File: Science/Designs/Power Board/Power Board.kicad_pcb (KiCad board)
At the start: 2 copper layers, 102.7 x 89.4 mm, 31 parts, among them P1 PWR_IN, P2 MOTOR_PWR_OUT, P3 MAIN_PWR_OUT, P4 I2C, P5 MOTOR_SW, P6 REG_12V, P7 REG_5V, U1 INA219, U2 INA219, U3 INA219

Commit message: squeezed
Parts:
- moved P7 1.78 mm to (165.4, 134.8)
- moved P3 1.78 mm to (165.4, 75.9)
- moved P6 1.78 mm to (165.4, 103.1)
- moved REF** 1.27 mm to (96.8, 106.7)
- moved REF** 1.27 mm to (96.8, 53.8)
- moved P1 0.92 mm to (108.5, 74.0)
- moved REF** 0.76 mm to (161.0, 53.1)
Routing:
- net +12V: track 80.2 -> 84.9 mm
- net +5V: track 62.8 -> 66.4 mm
- net /24V_IN: track 18.7 -> 15.6 mm
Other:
- board size 102.7 x 89.4 mm -> 99.4 x 89.4 mm

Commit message: Final changes
(I didn't save apparently)
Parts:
- moved G*** 6.59 mm to (157.2, 69.1)
- moved G*** 1.70 mm to (123.2, 73.2)
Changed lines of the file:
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@@
   )
   (module ScienceFootprints:Husky-0.50in (layer F.Cu)
-    (at 122.428 71.628)
+    (at 123.19 73.152)
     (fp_text reference G*** (at 0 0) (layer F.SilkS) hide
       (effects (font (thickness 0.3)))
@@
   )
   (module ScienceFootprints:Scarlet-0.25in (layer F.Cu)
-    (at 163.068 72.136)
+    (at 157.226 69.088)
     (fp_text reference G*** (at 0 0) (layer F.SilkS) hide
       (effects (font (thickness 0.3)))
@@
   (gr_line (start 191.008 133.096) (end 191.008 54.356) (layer Edge.Cuts) (width 0.15))
   (gr_line (start 96.266 138.176) (end 185.928 138.176) (layer Edge.Cuts) (width 0.15))
-  (gr_text I2C (at 152.654 61.976) (layer F.SilkS)
-    (effects (font (size 1.5 1.5) (thickness 0.3)))
-  )
-  (gr_text "Power Input" (at 98.044 66.04 90) (layer F.SilkS)
-    (effects (font (size 1.5 1.5) (thickness 0.3)))
-  )
-  (gr_text GND (at 111.76 75.184 180) (layer F.SilkS)
-    (effects (font (size 1.5 1.5) (thickness 0.3)))
-  )
-  (gr_text +24V (at 103.632 75.184 180) (layer F.SilkS)
-    (effects (font (size 1.5 1.5) (thickness 0.3)))
-  )
-  (gr_text "Science Power Distribution Board\nHusky Robotics 2018\nJaden B/Cai B" (at 147.32 71.628) (layer F.SilkS)
+  (gr_text I2C (at 157.734 59.182 90) (layer F.SilkS)
+    (effects (font (size 1.5 1.5) (thickness 0.3)))
+  )
+  (gr_text "Power Input" (at 98.806 66.04 90) (layer F.SilkS)
+    (effects (font (size 1.5 1.5) (thickness 0.3)))
+  )
+  (gr_text GND (at 112.776 75.184 180) (layer F.SilkS)
+    (effects (font (size 1.5 1.5) (thickness 0.3)))
+  )
+  (gr_text +24V (at 104.902 75.184 180) (layer F.SilkS)
+    (effects (font (size 1.5 1.5) (thickness 0.3)))
+  )
+  (gr_text "Science Power Distribution Board\nHusky Robotics 2018\nJaden B/Cai B" (at 140.716 68.072) (layer F.SilkS)
     (effects (font (size 1.5 1.5) (thickness 0.3)))
   )
@@
     (effects (font (size 1.5 1.5) (thickness 0.3)))
   )
-  (gr_text GND (at 164.592 122.936 90) (layer F.SilkS)
-    (effects (font (size 1.5 1.5) (thickness 0.3)))
-  )
-  (gr_text +5V (at 164.592 115.316 90) (layer F.SilkS)
-    (effects (font (size 1.5 1.5) (thickness 0.3)))
-  )
-  (gr_text +24V (at 164.592 99.568 90) (layer F.SilkS)
-    (effects (font (size 1.5 1.5) (thickness 0.3)))
-  )
-  (gr_text GND (at 164.592 91.44 90) (layer F.SilkS)
+  (gr_text GND (at 164.338 122.936 90) (layer F.SilkS)
+    (effects (font (size 1.5 1.5) (thickness 0.3)))
+  )
+  (gr_text +5V (at 164.338 115.316 90) (layer F.SilkS)
+    (effects (font (size 1.5 1.5) (thickness 0.3)))
+  )
+  (gr_text +24V (at 164.338 99.568 90) (layer F.SilkS)
+    (effects (font (size 1.5 1.5) (thickness 0.3)))
+  )
+  (gr_text GND (at 164.338 91.44 90) (layer F.SilkS)
     (effects (font (size 1.5 1.5) (thickness 0.3)))
   )
@@
     (effects (font (size 1.5 1.5) (thickness 0.3)))
   )
-  (gr_text GND (at 164.592 64.008 90) (layer F.SilkS)
-    (effects (font (size 1.5 1.5) (thickness 0.3)))
-  )
+  (gr_text GND (at 164.338 64.008 90) (layer F.SilkS)
+    (effects (font (size 1.5 1.5) (thickness 0.3)))
+  )

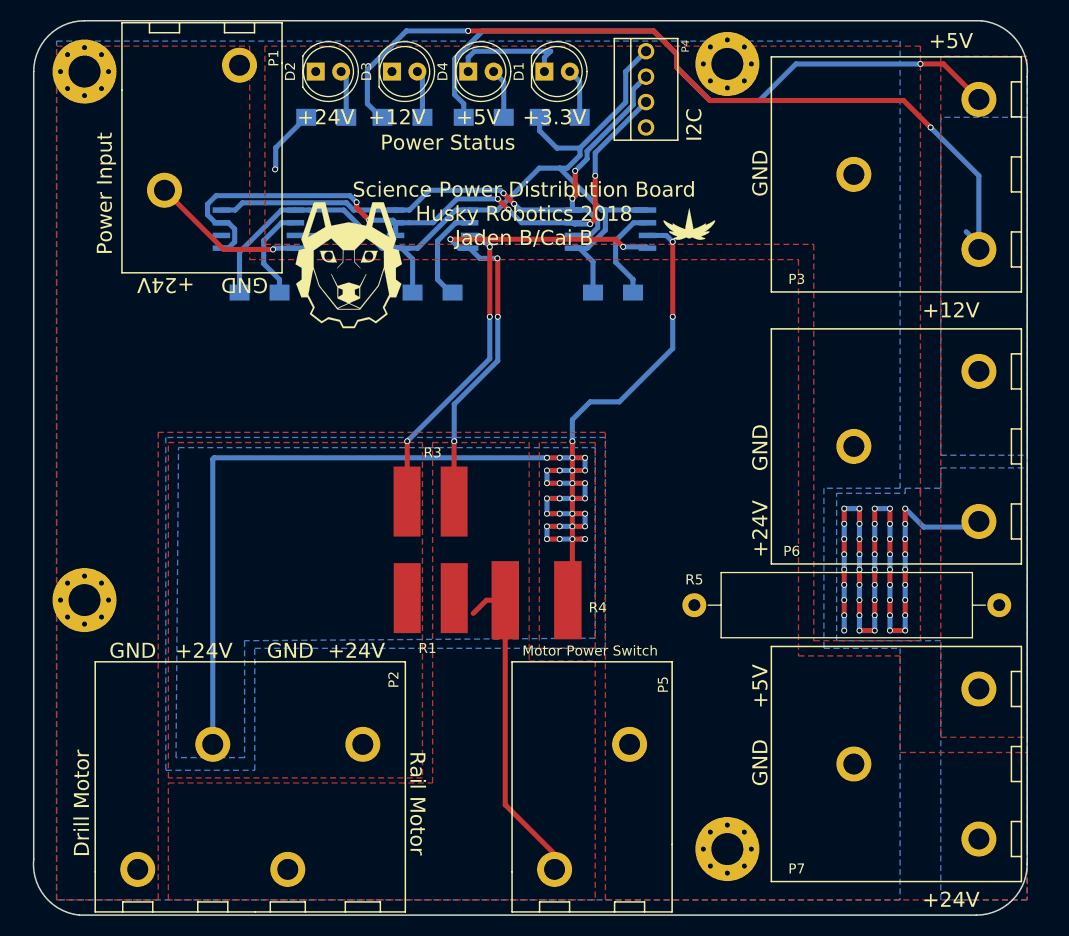
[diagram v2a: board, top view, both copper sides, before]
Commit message: Replaced current sensor with INA226
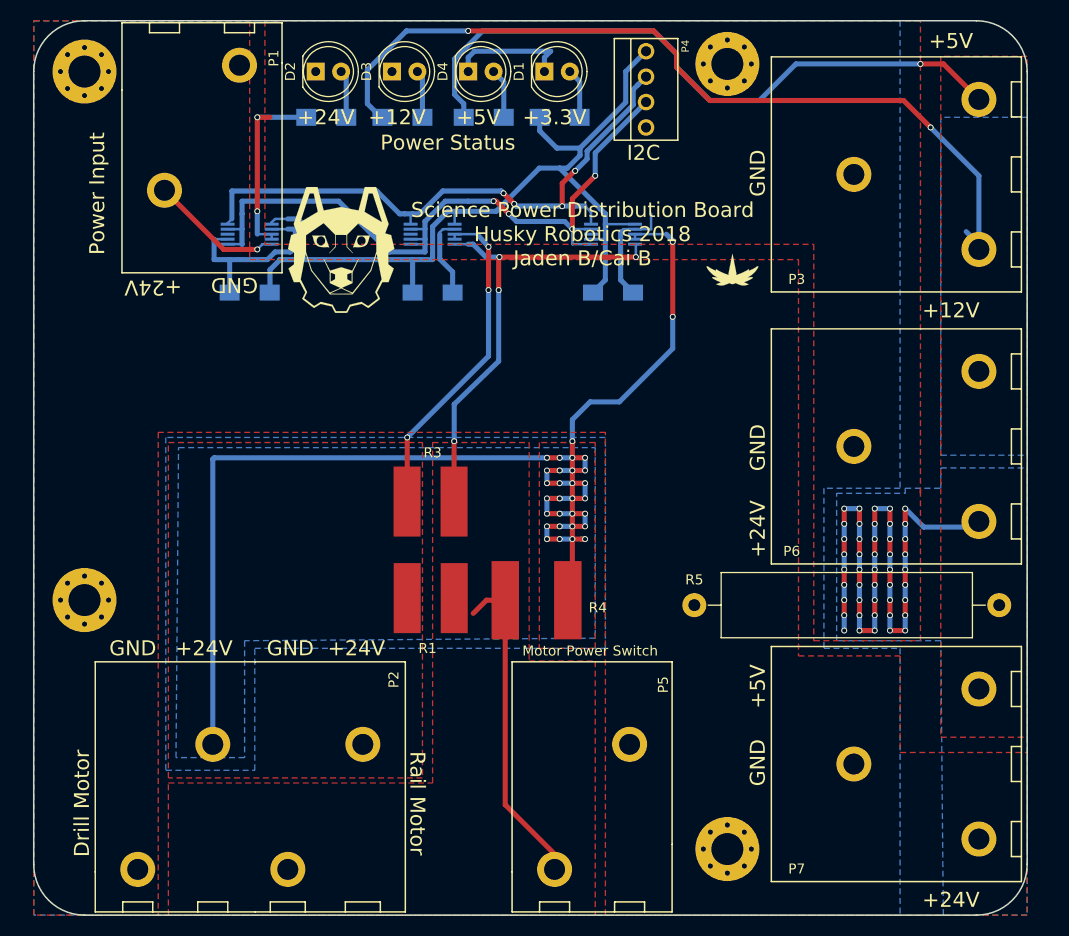
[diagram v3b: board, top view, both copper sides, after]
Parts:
- U1, U2, U3: value INA219 -> INA226; footprint Housings_SOIC:SO-8_5.3x6.2mm_Pitch1.27mm -> Housings_SSOP:MSOP-10_3x3mm_Pitch0.5mm
- moved G*** 6.29 mm to (161.5, 73.7)
- moved G*** 1.70 mm to (122.4, 71.6)
- moved U3 1.01 mm to (113.3, 70.1)
- moved C2 0.98 mm to (113.3, 75.9), turned to 180 degrees
- moved U2 0.57 mm to (149.6, 70.1)
- moved U1 0.51 mm to (131.6, 70.1)
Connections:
- U1 pad 1: +3V3 -> /I2C_SDA
- U1 pad 3: /I2C_SDA -> Net-(U1-Pad3)
- U1 pad 4: /I2C_SCL -> /I2C_SDA
- U1 pad 5: +3V3 -> /I2C_SCL
- U1 pad 6: GND -> +3V3
- U1 pad 7: Net-(P2-Pad4) -> GND
- U1 pad 8: Net-(P5-Pad1) -> Net-(P2-Pad4)
- U2 pad 1: +3V3 -> /I2C_SDA
- U2 pad 2: /I2C_SCL -> +3V3
- U2 pad 3: /I2C_SDA -> Net-(U2-Pad3)
- U2 pad 4: /I2C_SCL -> /I2C_SDA
- U2 pad 5: +3V3 -> /I2C_SCL
- U2 pad 6: GND -> +3V3
- U2 pad 7: Net-(P2-Pad2) -> GND
- U2 pad 8: Net-(P5-Pad1) -> Net-(P2-Pad2)
- U3 pad 3: /I2C_SDA -> Net-(U3-Pad3)
- U3 pad 4: /I2C_SCL -> /I2C_SDA
- U3 pad 5: +3V3 -> /I2C_SCL
- U3 pad 6: GND -> +3V3
- U3 pad 7: +24V -> GND
- U3 pad 8: /24V_IN -> +24V
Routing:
- net +24V: track 85.2 -> 95.9 mm
- net GND: track 41.7 -> 51.4 mm
- net /I2C_SDA: track 65.1 -> 72.7 mm, vias 6 -> 4
- net Net-(P5-Pad1): track 82.9 -> 77.5 mm, vias 5 -> 4
- net +3V3: track 93.4 -> 90.5 mm
- net /24V_IN: track 15.6 -> 13.4 mm
- net Net-(P2-Pad4): track 31.4 -> 33.3 mm
- net Net-(P2-Pad2): track 141.2 -> 142.5 mm
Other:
- board size 99.4 x 89.4 mm -> 99.3 x 89.4 mm

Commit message: Added Labels
PDB is officially done
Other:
- board text added: "24V to 12V Converter"
- board text added: "24V to 5V Converter"
- board text added: "5V/12V Out"
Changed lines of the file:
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@@
     (area 91.618999 48.692999 191.083001 138.251001)
     (thickness 1.6)
-    (drawings 33)
+    (drawings 36)
     (tracks 431)
     (zones 0)
@@
     )
   )
+  (gr_text "24V to 5V Converter" (at 171.704 135.89) (layer F.SilkS)
+    (effects (font (size 1 1) (thickness 0.1)))
+  )
+  (gr_text "5V/12V Out" (at 169.672 51.562) (layer F.SilkS)
+    (effects (font (size 1 1) (thickness 0.1)))
+  )
+  (gr_text "24V to 12V Converter" (at 171.704 78.74 360) (layer F.SilkS)
+    (effects (font (size 1 1) (thickness 0.1)))
+  )
   (gr_arc (start 96.774 133.096) (end 96.774 138.176) (angle 90) (layer Edge.Cuts) (width 0.15))
